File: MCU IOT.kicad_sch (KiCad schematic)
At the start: 0 parts

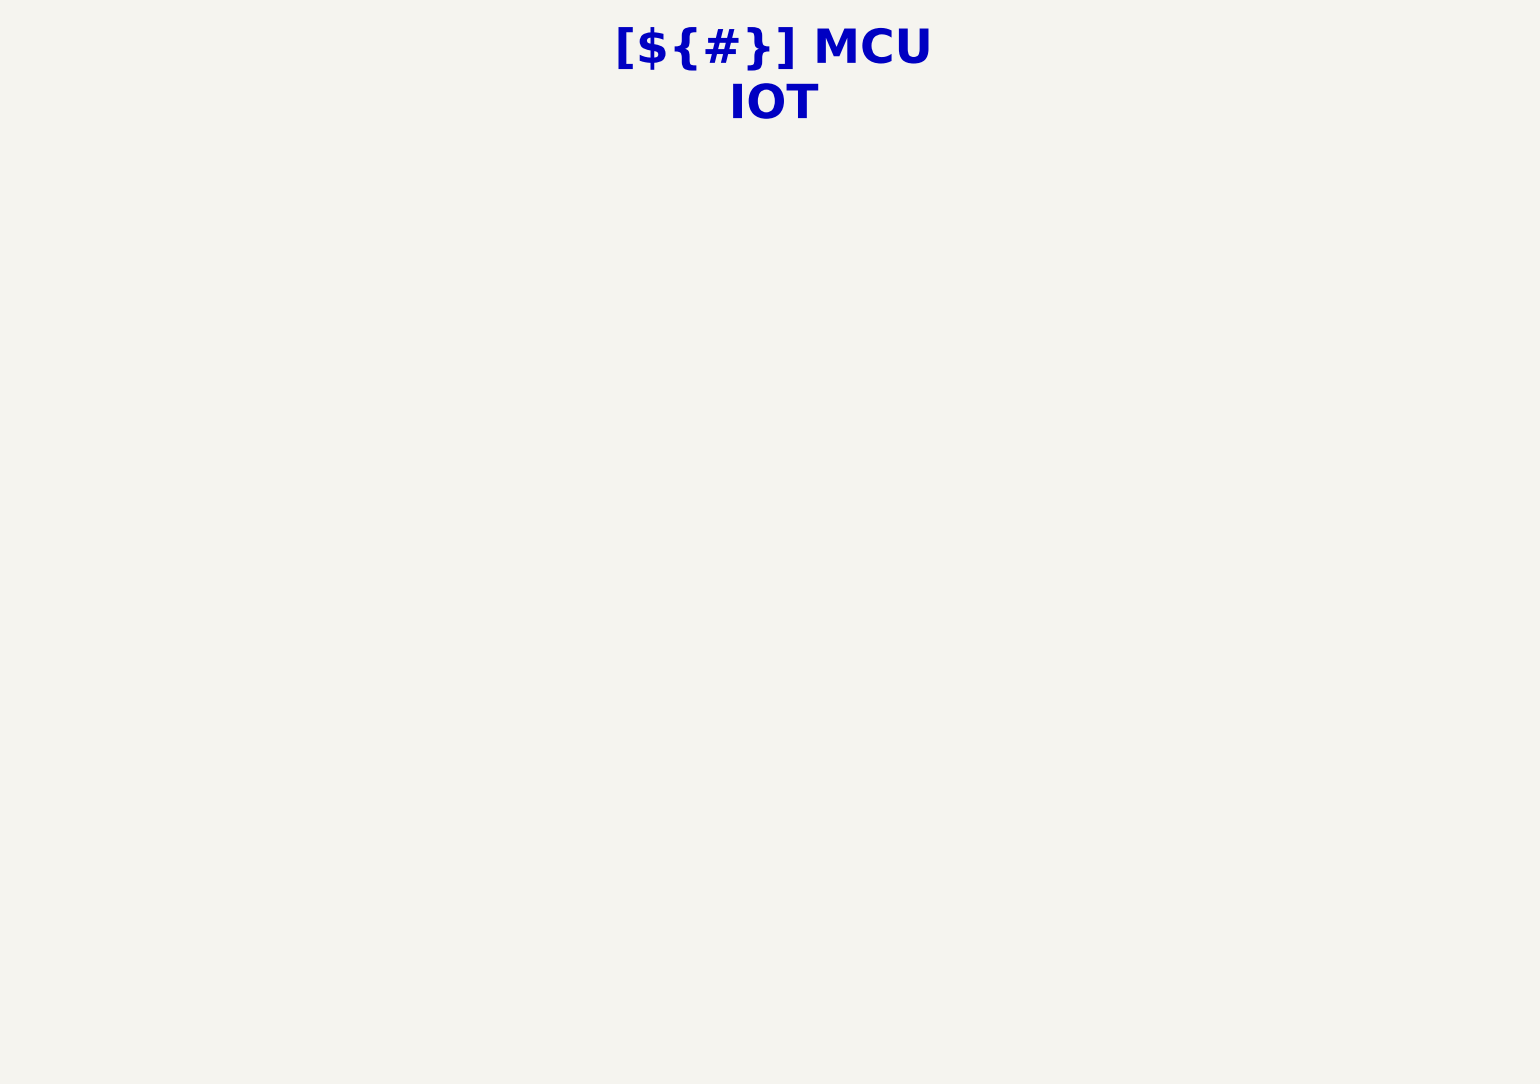
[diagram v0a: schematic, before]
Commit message: [Schematic][Add] MCU IOT, add schematic
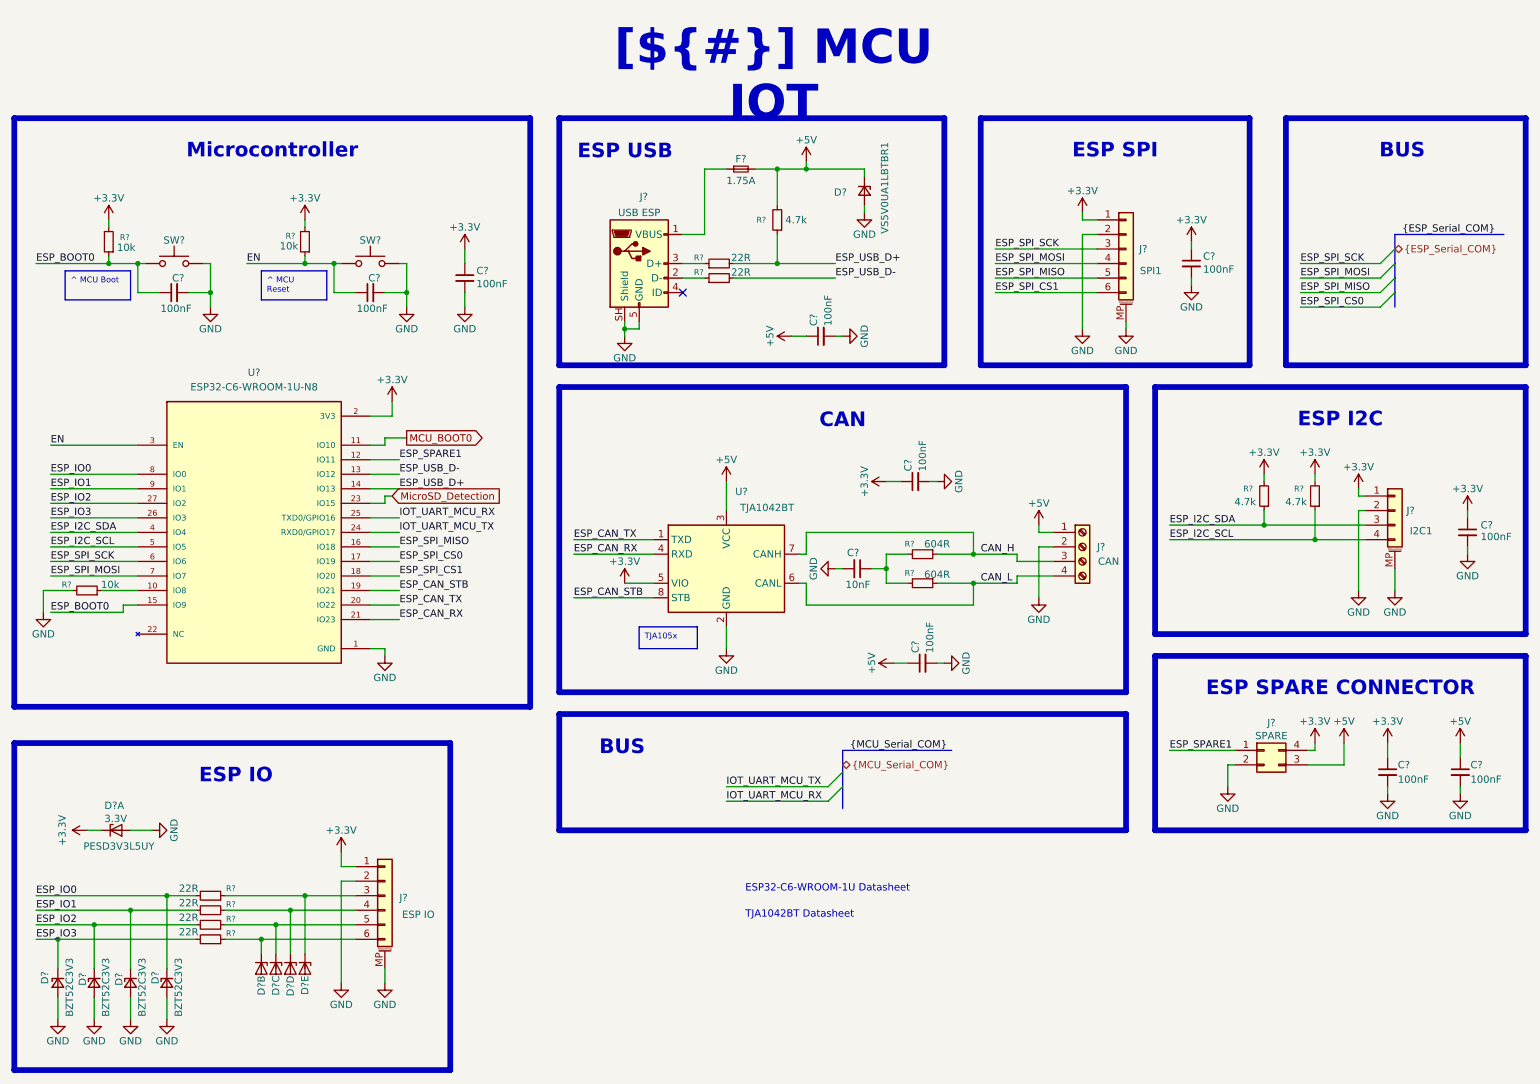
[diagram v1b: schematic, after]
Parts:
- added C? (x10): 100nF, Capacitor_SMD:C_0603_1608Metric_Pad1.08x0.95mm_HandSolder, symbol Device:C_Small
- added C?: 10nF, Capacitor_SMD:C_0603_1608Metric_Pad1.08x0.95mm_HandSolder, symbol Device:C_Small
- added D? (x5): 3.3V, Package_TO_SOT_SMD:SOT-363_SC-70-6, symbol Power_Protection:PESD3V3L5UY
- added D? (x4): 3.3V, Diode_SMD:D_SOD-123F, symbol Device:D_Zener_Small
- added D?: 5V, Diode_SMD:D_SMB, symbol Device:D_Zener_Small
- added F?: 1.75A, Fuse:Fuse_0603_1608Metric, symbol Device:Fuse_Small
- added J?: *, TerminalBlock_Phoenix:TerminalBlock_Phoenix_MPT-0,5-4-2.54_1x04_P2.54mm_Horizontal, symbol Connector:Screw_Terminal_01x04
- added J?: *, Connector_JST:JST_PH_S4B-PH-SM4-TB_1x04-1MP_P2.00mm_Horizontal, symbol Connector_Generic_MountingPin:Conn_01x04_MountingPin
- added J?: Conn_02x02_Counter_Clockwise, Connector_Molex:Molex_Micro-Fit_3.0_43045-0412_2x02_P3.00mm_Vertical, symbol Connector_Generic:Conn_02x02_Counter_Clockwise
- added J? (x2): *, Connector_JST:JST_PH_S6B-PH-SM4-TB_1x06-1MP_P2.00mm_Horizontal, symbol Connector_Generic_MountingPin:Conn_01x06_MountingPin
- added J?: *, Connector_USB:USB_B_Amphenol_MUSB-D511_Vertical_Rugged, symbol Connector:USB_B_Micro
- added R? (x4): 22R, Resistor_SMD:R_0805_2012Metric_Pad1.20x1.40mm_HandSolder, symbol Device:R_Small
- added R? (x2): 22R, Resistor_SMD:R_0603_1608Metric_Pad0.98x0.95mm_HandSolder, symbol Device:R_Small
- added R? (x2): 604R, Resistor_SMD:R_0603_1608Metric_Pad0.98x0.95mm_HandSolder, symbol Device:R_Small
- added R? (x3): 4.7k, Resistor_SMD:R_0603_1608Metric_Pad0.98x0.95mm_HandSolder, symbol Device:R_Small
- added R? (x3): 10k, Resistor_SMD:R_0603_1608Metric_Pad0.98x0.95mm_HandSolder, symbol Device:R_Small
- added SW? (x2): *, Button_Switch_SMD:SW_SPST_CK_RS282G05A3, symbol Switch:SW_Push
- added U?: *, P_MCU:XCVR_ESP32-C6-WROOM-1U-N8, symbol P_MCU:ESP32-C6-WROOM-1U-N4
- added U?: *, Package_SO:SOIC-8_3.9x4.9mm_P1.27mm, symbol Interface_CAN_LIN:TJA1042T-3
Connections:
- new net: D?.6 (K5), J?.3 (Pin_3), R?.1
- new net: D?.5 (K4), J?.4 (Pin_4), R?.1
- new net: J?.2 (D-), R?.1
- new net: C?.1, R?.2, R?.2
- new net: D?.4 (K3), J?.5 (Pin_5), R?.1
- new net: F?.1, J?.1 (VBUS)
- new net: D?.3 (K2), J?.6 (Pin_6), R?.1
- new net: J?.3 (D+), R?.1
- new net: R?.1, U?.10 (IO8)
- new net +3.3V: C?.1, C?.1, C?.1, C?.1, C?.1, D?.1 (K1), J?.1 (Pin_1), J?.1 (Pin_1), J?.1 (Pin_1), J?.4 (Pin_4), R?.2, R?.2, R?.2, R?.2, U?.2 (3V3), U?.5 (VIO)
- new net +5V: C?.1, C?.1, C?.1, D?.1 (K), F?.2, J?.1 (Pin_1), J?.3 (Pin_3), R?.2, U?.3 (VCC)
- new net CAN_H: J?.3 (Pin_3), R?.1, U?.7 (CANH)
- new net CAN_L: J?.4 (Pin_4), R?.1, U?.6 (CANL)
- new net EN: C?.1, R?.1, SW?.1, U?.3 (EN)
- new net ESP_BOOT0: C?.1, R?.1, SW?.1, U?.15 (IO9)
- new net ESP_CAN_RX: U?.21 (IO23), U?.4 (RXD)
- new net ESP_CAN_STB: U?.19 (IO21), U?.8 (STB)
- new net ESP_CAN_TX: U?.1 (TXD), U?.20 (IO22)
- new net ESP_I2C_SCL: J?.4 (Pin_4), R?.1, U?.5 (IO5)
- new net ESP_I2C_SDA: J?.3 (Pin_3), R?.1, U?.4 (IO4)
- new net ESP_IO0: D?.1 (K), R?.2, U?.8 (IO0)
- new net ESP_IO1: D?.1 (K), R?.2, U?.9 (IO1)
- new net ESP_IO2: D?.1 (K), R?.2, U?.27 (IO2)
- new net ESP_IO3: D?.1 (K), R?.2, U?.26 (IO3)
- new net ESP_SPARE1: J?.1 (Pin_1), U?.12 (IO11)
- new net ESP_SPI_CS0: U?.17 (IO19)
- new net ESP_SPI_CS1: J?.6 (Pin_6), U?.18 (IO20)
- new net ESP_SPI_MISO: J?.5 (Pin_5), U?.16 (IO18)
- new net ESP_SPI_MOSI: J?.4 (Pin_4), U?.7 (IO7)
- new net ESP_SPI_SCK: J?.3 (Pin_3), U?.6 (IO6)
- new net ESP_USB_D+: R?.1, R?.2, U?.14 (IO13)
- new net ESP_USB_D-: R?.2, U?.13 (IO12)
- new net GND: C?.2, C?.2, C?.2, C?.2, C?.2, C?.2, C?.2, C?.2, C?.2, C?.2, C?.2, D?.2 (A), D?.2 (A), D?.2 (A), D?.2 (A), D?.2 (A), D?.2 (A), J?.2 (Pin_2), J?.2 (Pin_2), J?.2 (Pin_2), J?.2 (Pin_2), J?.2 (Pin_2), J?.5 (GND), J?.MP (MountPin), J?.MP (MountPin), J?.MP (MountPin), J?.SH (Shield), R?.2, SW?.2, SW?.2, U?.1 (GND), U?.2 (GND), U?.28 (GND), U?.29_1 (GND), U?.29_2 (GND), U?.29_3 (GND), U?.29_4 (GND), U?.29_5 (GND), U?.29_6 (GND), U?.29_7 (GND), U?.29_8 (GND), U?.29_9 (GND)
- new net IOT_UART_MCU_RX: U?.25 (TXD0/GPIO16)
- new net IOT_UART_MCU_TX: U?.24 (RXD0/GPIO17)
- new net MCU_BOOT0: U?.11 (IO10)
- new net MicroSD_Detection: U?.23 (IO15)
- no-connect marks 0 -> 1
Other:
- note added: "ESP32-C6-WROOM-1U Datasheet"
- note added: "TJA1042BT Datasheet"

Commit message: [Schematic][Modify] Annotation of all  the components
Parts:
- gave numbers to parts that had none: 42

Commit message: [Schematic][Modify] Annotation of all  the components
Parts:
- renumbered C26 to C19, C21 to C20, C19 to C21, C20 to C22, C22 to C23, C29 to C25, C23 to C26, C25 to C27, C27 to C28, C28 to C29, D9 to D10, D10 to D5, D7 to D6, D5 to D7, D6 to D8, D8 to D9, J5 to J10, J8 to J5, J10 to J7, J7 to J8, R23 to R14, R20 to R16, R21 to R17, R22 to R18, R26 to R19, R27 to R20, R24 to R21, R25 to R22, R14 to R23, R16 to R24, R17 to R25, R18 to R26, R19 to R27
